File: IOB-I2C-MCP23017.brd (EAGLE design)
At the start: 71.1 x 33 mm, 10 parts, among them IC1 MCP23017SO

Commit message: cleanup
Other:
- board text added: "Input Changed"
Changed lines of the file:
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@@
 <layer number="90" name="Modules" color="5" fill="1" visible="no" active="no"/>
 <layer number="104" name="Name" color="16" fill="1" visible="no" active="no"/>
-<layer number="125" name="_tNames" color="14" fill="1" visible="yes" active="yes"/>
-<layer number="204" name="_Name" color="5" fill="10" visible="yes" active="yes"/>
+<layer number="125" name="_tNames" color="14" fill="1" visible="no" active="yes"/>
+<layer number="204" name="_Name" color="5" fill="10" visible="no" active="yes"/>
 </layers>
 <board>
@@
 <wire x1="67.31" y1="16.51" x2="67.31" y2="1.27" width="2.1844" layer="22"/>
 <text x="21.59" y="13.335" size="0.6096" layer="125" font="vector">C1</text>
-<text x="28.194" y="26.924" size="1.778" layer="125" font="vector" ratio="10">IC1</text>
-<text x="36.83" y="26.035" size="1.27" layer="125" font="vector" rot="R180">LED1</text>
+<text x="37.846" y="20.574" size="1.778" layer="125" font="vector" ratio="10" rot="R90">IC1</text>
+<text x="43.18" y="27.305" size="1.27" layer="125" font="vector" rot="R180">LED1</text>
 <text x="42.799" y="7.62" size="0.8128" layer="125" font="vector" rot="R270">R1</text>
 <text x="50.546" y="9.652" size="0.8128" layer="125" font="vector" rot="R90">R2</text>
@@
 <text x="-0.762" y="30.861" size="0.4064" layer="204" font="vector" rot="R270">U$5</text>
 <text x="50.038" y="30.861" size="0.4064" layer="204" font="vector" rot="R270">U$5</text>
+<text x="28.067" y="26.289" size="0.8128" layer="21">Input
+Changed</text>
+<wire x1="35.56" y1="15.24" x2="35.56" y2="19.05" width="0.4064" layer="21"/>
+<wire x1="35.56" y1="19.05" x2="36.83" y2="17.78" width="0.4064" layer="21"/>
+<wire x1="35.56" y1="19.05" x2="34.29" y2="17.78" width="0.4064" layer="21"/>
 </plain>
 <attributes>
@@
 <attribute name="OC_NEWARK" value="31K2958" x="34.798" y="17.145" size="1.778" layer="27" font="vector" ratio="10" rot="R270" display="off"/>
 <attribute name="OC_FARNELL" value="1332087" x="34.798" y="17.145" size="1.778" layer="27" font="vector" ratio="10" rot="R270" display="off"/>
-<attribute name="NAME" x="28.194" y="26.924" size="1.778" layer="25" ratio="10"/>
-<attribute name="VALUE" x="34.417" y="8.509" size="1.778" layer="27" ratio="10" rot="R90"/>
+<attribute name="NAME" x="37.846" y="20.574" size="1.778" layer="25" ratio="10" rot="R90"/>
+<attribute name="VALUE" x="33.782" y="8.509" size="1.778" layer="27" ratio="10" rot="R90"/>
 </element>
 <element name="SW1" library="SPCoast" package="EDG-04" value="" x="60.96" y="13.97" smashed="yes" rot="R180">
@@
 <element name="U$5" library="SPCoast" package="I2C-EXPANDER" value="I2C-EXPANDER" x="35.56" y="27.94"/>
 <element name="C1" library="SPCoast" package="0603-CAP" value="0.1uF" x="22.86" y="12.065"/>
-<element name="LED1" library="SPCoast" package="0805-LED" value="" x="35.56" y="27.305" rot="R180"/>
+<element name="LED1" library="SPCoast" package="0805-LED" value="" x="35.56" y="27.305" smashed="yes" rot="R180">
+<attribute name="NAME" x="43.18" y="27.305" size="1.27" layer="25" rot="R180"/>
+<attribute name="VALUE" x="36.83" y="29.845" size="1.27" layer="27" rot="R180"/>
+</element>
 <element name="R4" library="SPCoast" package="0603-RES" value="2k2" x="35.56" y="29.845"/>
 </elements>
@@
 </board>
 </drawing>
+<compatibility>
+<note version="6.3" minversion="6.2.2" severity="warning">
+Since Version 6.2.2 text objects can contain more than one line,
+which will not be processed correctly with this version.
+</note>
+</compatibility>
 </eagle>

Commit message: cleanup layout
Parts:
- BOARD: value I2C-EXPANDER -> CONNECTOR-I2C-EXPANDER
- LED1: value (none) -> G
- R4: value 2k2 -> 4k7
- moved R4 4.49 mm to (31.5, 27.9), turned to 180 degrees
- moved SW1 1.27 mm to (59.7, 14.0)
- moved LED1 0.64 mm to (35.6, 27.9)
- moved OSHW1 0.40 mm to (35.1, 4.19)
- renumbered U$5 to BOARD
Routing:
- net SDA: track 51.3 -> 78.1 mm, vias 1 -> 3
- net SCL: track 75.6 -> 79.5 mm
- net A1: track 39.3 -> 36.8 mm
- net P4: track 25.7 -> 24.2 mm
- net A3: track 24.0 -> 22.7 mm
- net A0: track 29.1 -> 27.9 mm
- net P13: track 24.1 -> 23.0 mm
- net P3: track 30.8 -> 29.8 mm
- net P14: track 29.3 -> 28.5 mm
- net N$2: track 16.1 -> 16.7 mm
- net P2: track 37.7 -> 37.0 mm
- net P9: track 26.2 -> 25.7 mm
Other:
- board text added: "BOARD"
- board text added: "I2C Address"
- board text added: "MCP23017SO"
- board text added: "SO28-W"
- board text added: "Solder"
- board text removed: "Address"
- board text removed: "Board I2C"
- board text removed: "U$5"

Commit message: added missing values
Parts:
- SW1: value (none) -> SPSTx4
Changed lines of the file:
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@@
 <attribute name="VALUE" x="42.672" y="9.779" size="1.27" layer="27" ratio="10" rot="R90"/>
 </element>
-<element name="SW1" library="SPCoast" package="EDG-04" value="" x="59.69" y="13.97" smashed="yes" rot="R180">
+<element name="SW1" library="SPCoast" package="EDG-04" value="SPSTx4" x="59.69" y="13.97" smashed="yes" rot="R180">
 <attribute name="VALUE" x="65.532" y="20.574" size="1.27" layer="27" ratio="10" rot="R180"/>
 <attribute name="NAME" x="52.324" y="16.002" size="1.27" layer="25" ratio="10" rot="R270"/>

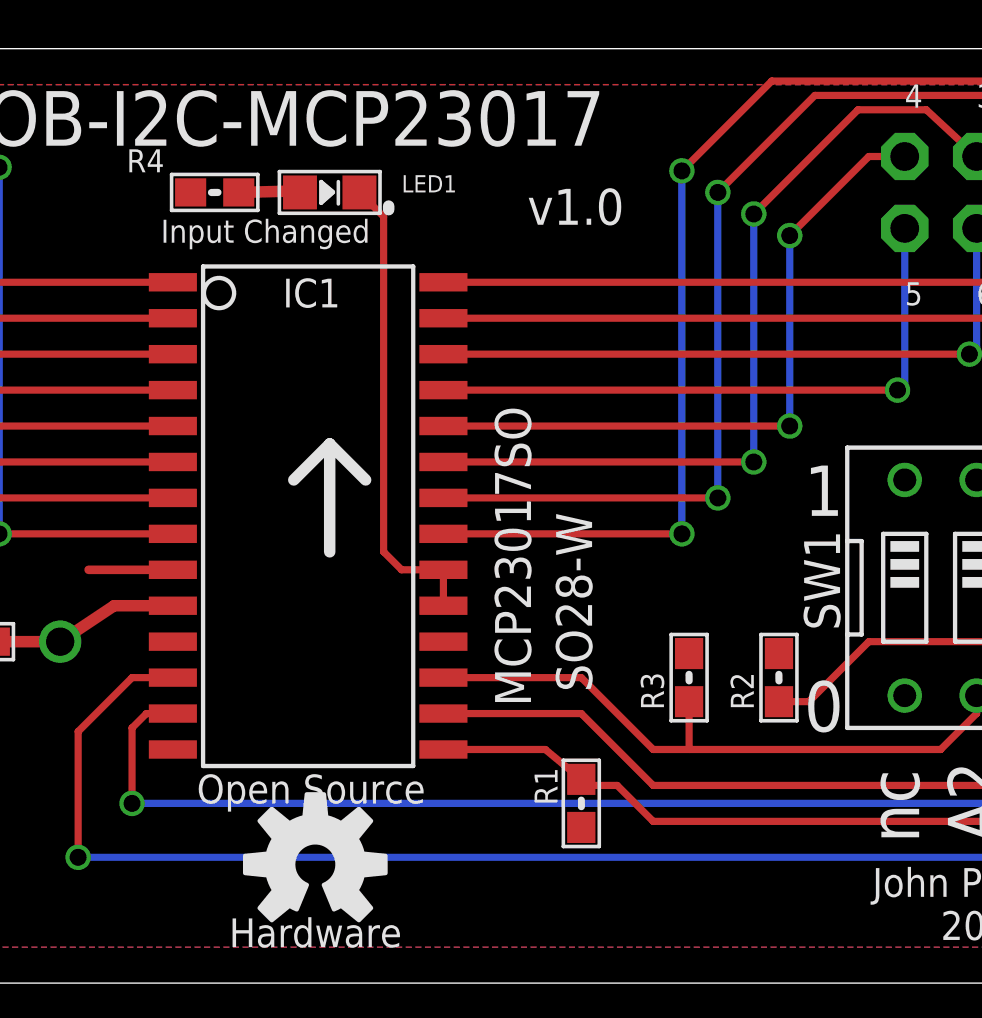
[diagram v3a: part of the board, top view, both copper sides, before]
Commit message: normalized values
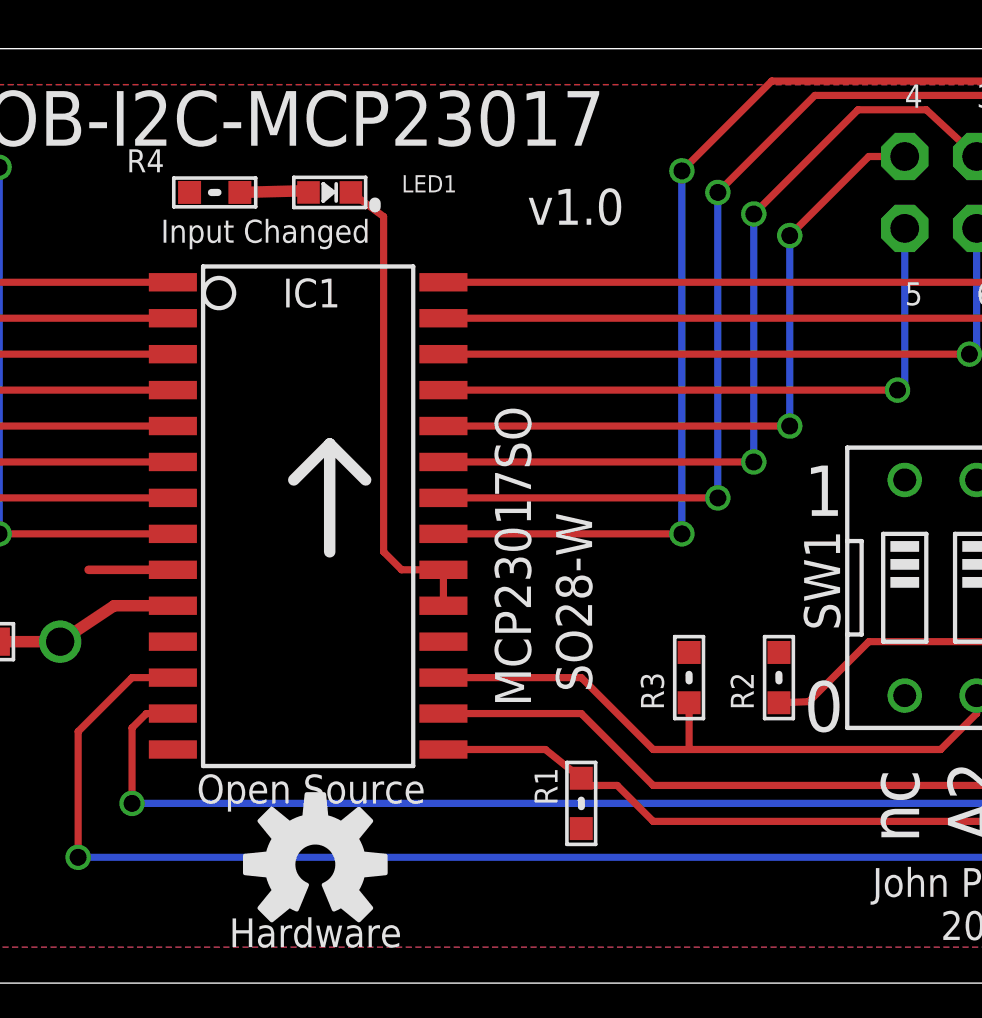
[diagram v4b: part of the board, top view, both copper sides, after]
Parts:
- LED1: device SPCoast:0805-LED -> SPCoast:0603-LED
- OSHW1: value DOC-OSHW-LOGO-M -> OSHW
